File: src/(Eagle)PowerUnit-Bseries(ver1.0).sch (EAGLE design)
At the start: 53 parts, among them CON1 XT90PW-M, CON2 XT90PW-F, CON3 XT60PW-F, CON4 XT60PW-F, CON5 XT60PW-F, CON6 XT60PW-F, U1 LQFP64, U2 MCP2517FD, U3 CH340E, U4 AP63203WU-7

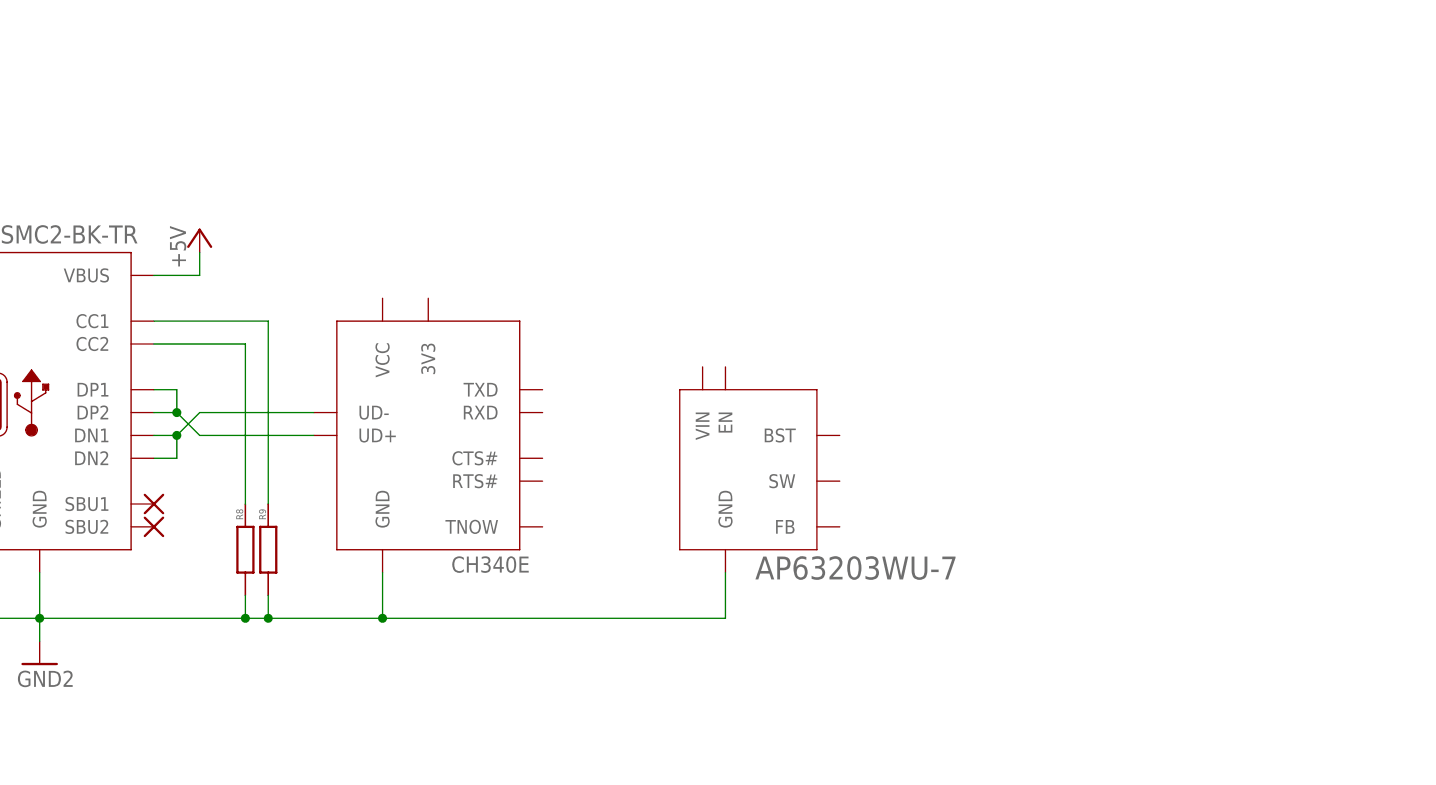
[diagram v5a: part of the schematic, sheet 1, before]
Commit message: 5Vレギュレータの追加など
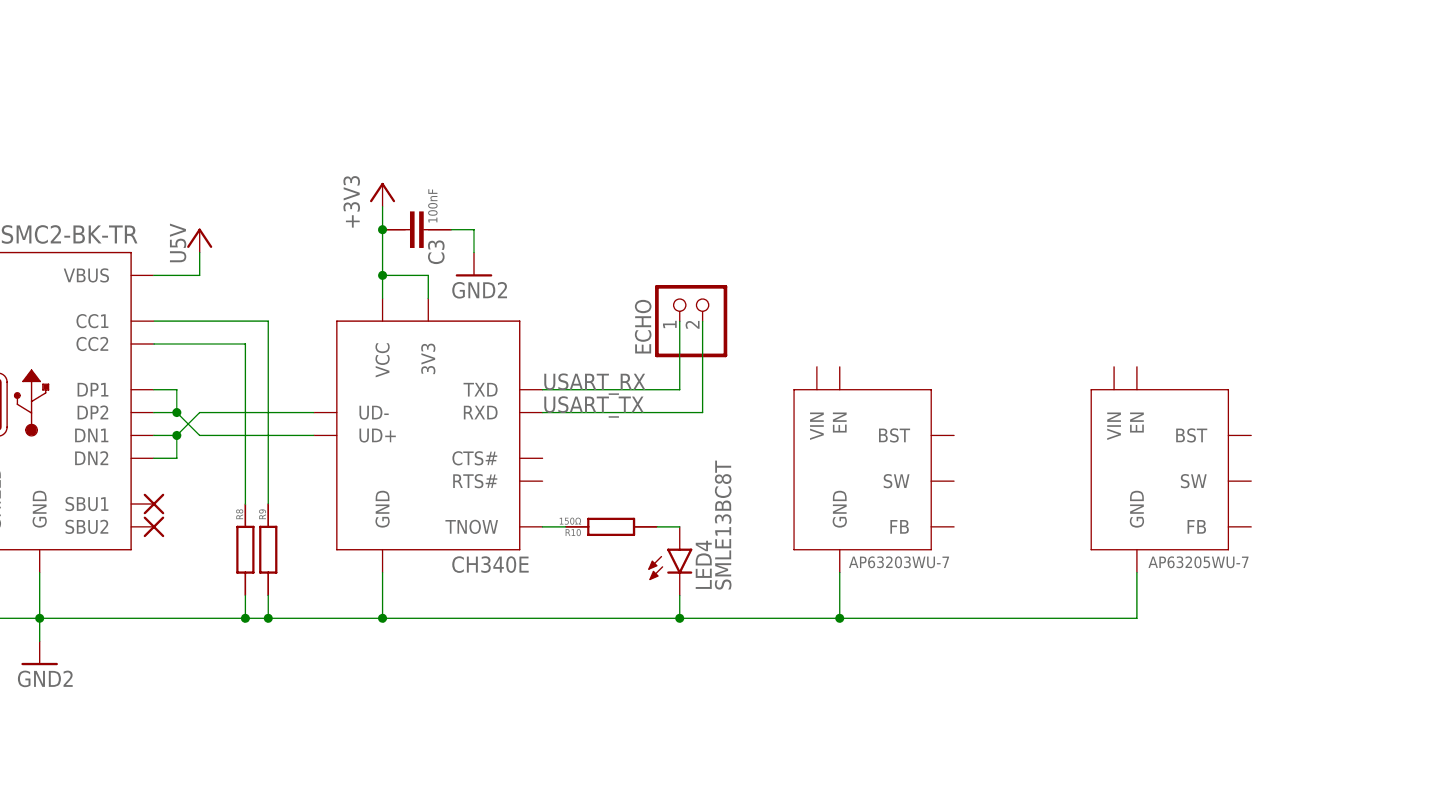
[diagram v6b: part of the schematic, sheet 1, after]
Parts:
- added C3: GCM188L81H104KA57, GCM188L81H104K57(0.1uF):GCM188L81H104KA57
- added ECHO: (no value), pinhead:PINHD-1X2
- added LED4: SMLE13BC8T, SML-E12V8WT86:SML-E12V8WT86
- added R10: 150Ω, CR0603:CR0603
- added U5: AP63205WU-7, AP63205WU-7:AP63205WU-7
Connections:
- net +5V renamed U5V
- new net +3V3: C3.P$2, U3.3V3, U3.VCC
- new net N$33: R10.RIGHT, U3.TNOW
- new net N$34: LED4.A, R10.LEFT
- new net USART_RX: ECHO.1, U1.P17, U3.TXD
- new net USART_TX: ECHO.2, U1.P16, U3.RXD
- net GND2: now also C3.P$1, LED4.C, U5.GND
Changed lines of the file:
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@@
 <part name="U3" library="CH340E" deviceset="CH340E" device=""/>
 <part name="U4" library="AP63203WU-7" deviceset="AP63203WU-7" device=""/>
+<part name="U5" library="AP63205WU-7" deviceset="AP63205WU-7" device=""/>
+<part name="ECHO" library="pinhead" library_urn="urn:adsk.eagle:library:325" deviceset="PINHD-1X2" device="" package3d_urn="urn:adsk.eagle:package:22435/2"/>
+<part name="C3" library="GCM188L81H104K57(0.1uF)" deviceset="GCM188L81H104KA57" device=""/>
+<part name="GND2" library="supply1" library_urn="urn:adsk.eagle:library:371" deviceset="GND" device=""/>
+<part name="+3V1" library="supply1" library_urn="urn:adsk.eagle:library:371" deviceset="+3V3" device=""/>
+<part name="R10" library="CR0603" deviceset="CR0603" device="" value="150Ω"/>
+<part name="LED4" library="SML-E12V8WT86" deviceset="SML-E12V8WT86" device="" value="SMLE13BC8T"/>
 </parts>
 <sheets>
@@
 <instance part="U$2" gate="G$1" x="119.38" y="101.6" smashed="yes"/>
 <instance part="U$3" gate="G$1" x="119.38" y="104.14" smashed="yes"/>
-<instance part="P+5" gate="1" x="124.46" y="134.62" smashed="yes">
-<attribute name="VALUE" x="122.936" y="130.302" size="1.778" layer="96" rot="R90"/>
-</instance>
+<instance part="P+5" gate="1" x="124.46" y="134.62" smashed="yes"/>
 <instance part="R8" gate="G$1" x="129.54" y="99.06" smashed="yes" rot="R90">
 <attribute name="NAME" x="129.286" y="102.362" size="0.762" layer="95" rot="R90"/>
@@
 <attribute name="VALUE" x="152.4" y="96.52" size="1.778" layer="96"/>
 </instance>
-<instance part="U4" gate="G$1" x="177.8" y="99.06" smashed="yes">
-<attribute name="VALUE" x="186.182" y="95.758" size="2.54" layer="96"/>
+<instance part="U4" gate="G$1" x="190.5" y="99.06" smashed="yes">
+<attribute name="VALUE" x="196.596" y="97.028" size="1.27" layer="96"/>
+</instance>
+<instance part="U5" gate="G$1" x="223.52" y="99.06" smashed="yes">
+<attribute name="VALUE" x="229.87" y="97.028" size="1.27" layer="96"/>
+</instance>
+<instance part="ECHO" gate="G$1" x="180.34" y="127" smashed="yes" rot="R90">
+<attribute name="NAME" x="174.625" y="120.65" size="1.778" layer="95" rot="R90"/>
+<attribute name="VALUE" x="185.42" y="120.65" size="1.778" layer="96" rot="R90"/>
+</instance>
+<instance part="C3" gate="G$1" x="149.86" y="134.62" smashed="yes" rot="R270">
+<attribute name="NAME" x="149.86" y="133.604" size="1.778" layer="95" rot="R270"/>
+</instance>
+<instance part="GND2" gate="1" x="154.94" y="129.54" smashed="yes"/>
+<instance part="+3V1" gate="G$1" x="144.78" y="139.7" smashed="yes">
+<attribute name="VALUE" x="142.24" y="134.62" size="1.778" layer="96" rot="R90"/>
+</instance>
+<instance part="R10" gate="G$1" x="170.18" y="101.6" smashed="yes" rot="R180">
+<attribute name="NAME" x="166.878" y="101.346" size="0.762" layer="95" rot="R180"/>
+<attribute name="VALUE" x="166.878" y="102.616" size="0.762" layer="96" rot="R180"/>
+</instance>
+<instance part="LED4" gate="G$1" x="177.8" y="99.06" smashed="yes">
+<attribute name="NAME" x="181.356" y="94.488" size="1.778" layer="95" rot="R90"/>
+<attribute name="VALUE" x="183.515" y="94.488" size="1.778" layer="96" rot="R90"/>
 </instance>
 </instances>
@@
 <label x="104.14" y="83.82" size="1.778" layer="95"/>
 <pinref part="U4" gate="G$1" pin="GND"/>
-<wire x1="144.78" y1="91.44" x2="182.88" y2="91.44" width="0.1524" layer="91"/>
-<wire x1="182.88" y1="91.44" x2="182.88" y2="96.52" width="0.1524" layer="91"/>
+<wire x1="144.78" y1="91.44" x2="177.8" y2="91.44" width="0.1524" layer="91"/>
+<wire x1="177.8" y1="91.44" x2="195.58" y2="91.44" width="0.1524" layer="91"/>
+<wire x1="195.58" y1="91.44" x2="195.58" y2="96.52" width="0.1524" layer="91"/>
 <junction x="144.78" y="91.44"/>
+<pinref part="U5" gate="G$1" pin="GND"/>
+<wire x1="228.6" y1="96.52" x2="228.6" y2="91.44" width="0.1524" layer="91"/>
+<wire x1="228.6" y1="91.44" x2="195.58" y2="91.44" width="0.1524" layer="91"/>
+<junction x="195.58" y="91.44"/>
+<pinref part="LED4" gate="G$1" pin="C"/>
+<wire x1="177.8" y1="93.98" x2="177.8" y2="91.44" width="0.1524" layer="91"/>
+<junction x="177.8" y="91.44"/>
+</segment>
+<segment>
+<pinref part="C3" gate="G$1" pin="P$1"/>
+<wire x1="152.4" y1="134.62" x2="154.94" y2="134.62" width="0.1524" layer="91"/>
+<pinref part="GND2" gate="1" pin="GND"/>
+<wire x1="154.94" y1="134.62" x2="154.94" y2="132.08" width="0.1524" layer="91"/>
+<label x="152.4" y="127" size="1.778" layer="95"/>
 </segment>
 </net>
@@
 </segment>
 </net>
-<net name="+5V" class="0">
+<net name="U5V" class="0">
 <segment>
 <pinref part="USB1" gate="G$1" pin="VBUS"/>
@@
 <wire x1="119.38" y1="129.54" x2="124.46" y2="129.54" width="0.1524" layer="91"/>
 <wire x1="124.46" y1="129.54" x2="124.46" y2="132.08" width="0.1524" layer="91"/>
+<label x="122.936" y="130.81" size="1.778" layer="95" rot="R90"/>
 </segment>
 </net>
@@
 <pinref part="U3" gate="G$1" pin="UD-"/>
 <wire x1="124.46" y1="114.3" x2="137.16" y2="114.3" width="0.1524" layer="91"/>
+</segment>
+</net>
+<net name="USART_RX" class="0">
+<segment>
+<pinref part="U3" gate="G$1" pin="TXD"/>
+<wire x1="162.56" y1="116.84" x2="177.8" y2="116.84" width="0.1524" layer="91"/>
+<label x="162.56" y="116.84" size="1.778" layer="95"/>
+<pinref part="ECHO" gate="G$1" pin="1"/>
+<wire x1="177.8" y1="116.84" x2="177.8" y2="124.46" width="0.1524" layer="91"/>
+</segment>
+</net>
+<net name="USART_TX" class="0">
+<segment>
+<pinref part="U3" gate="G$1" pin="RXD"/>
+<wire x1="162.56" y1="114.3" x2="180.34" y2="114.3" width="0.1524" layer="91"/>
+<label x="162.56" y="114.3" size="1.778" layer="95"/>
+<pinref part="ECHO" gate="G$1" pin="2"/>
+<wire x1="180.34" y1="114.3" x2="180.34" y2="124.46" width="0.1524" layer="91"/>
+</segment>
+</net>
+<net name="+3V3" class="0">
+<segment>
+<pinref part="U3" gate="G$1" pin="VCC"/>
+<wire x1="144.78" y1="127" x2="144.78" y2="129.54" width="0.1524" layer="91"/>
+<wire x1="144.78" y1="129.54" x2="149.86" y2="129.54" width="0.1524" layer="91"/>
+<pinref part="U3" gate="G$1" pin="3V3"/>
+<wire x1="149.86" y1="129.54" x2="149.86" y2="127" width="0.1524" layer="91"/>
+<pinref part="C3" gate="G$1" pin="P$2"/>
+<wire x1="144.78" y1="129.54" x2="144.78" y2="134.62" width="0.1524" layer="91"/>
+<junction x="144.78" y="129.54"/>
+<pinref part="+3V1" gate="G$1" pin="+3V3"/>
+<wire x1="144.78" y1="137.16" x2="144.78" y2="134.62" width="0.1524" layer="91"/>
+<junction x="144.78" y="134.62"/>
+</segment>
+</net>
+<net name="N$33" class="0">
+<segment>
+<pinref part="R10" gate="G$1" pin="RIGHT"/>
+<pinref part="U3" gate="G$1" pin="TNOW"/>
+<wire x1="165.1" y1="101.6" x2="162.56" y2="101.6" width="0.1524" layer="91"/>
+</segment>
+</net>
+<net name="N$34" class="0">
+<segment>
+<pinref part="R10" gate="G$1" pin="LEFT"/>
+<pinref part="LED4" gate="G$1" pin="A"/>
+<wire x1="175.26" y1="101.6" x2="177.8" y2="101.6" width="0.1524" layer="91"/>
 </segment>
 </net>
@@
 </busses>
 <nets>
+<net name="USART_TX" class="0">
+<segment>
+<pinref part="U1" gate="G$1" pin="P16"/>
+<wire x1="106.68" y1="68.58" x2="88.9" y2="68.58" width="0.1524" layer="91"/>
+<label x="88.9" y="68.58" size="1.778" layer="95"/>
+</segment>
+</net>
+<net name="USART_RX" class="0">
+<segment>
+<pinref part="U1" gate="G$1" pin="P17"/>
+<wire x1="109.22" y1="63.5" x2="109.22" y2="43.18" width="0.1524" layer="91"/>
+<label x="109.22" y="43.18" size="1.778" layer="95" rot="R90"/>
+</segment>
+</net>
 </nets>
 </sheet>

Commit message: 理想ダイオード回路(ディスクリート)の追加
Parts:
- added GND, POW1: (no value), pinhead:PINHD-1X2
- added POW: 02-JST, con-jst-xh:02-JST
- added Q1, Q2, Q3: DMP3056L-7, DMP3056L-7:DMP3056L-7
- added R11, R12, R13, R14, R15, R18, R19, R20, R21, R22, R25, R26, R27, R28, R29: 10k, CR0603:CR0603
- added R16, R23, R30: 100k, CR0603:CR0603
- added R17, R24, R31: 0, CR0603:CR0603
- added U6, U7, U8: AP331AWG-7, AP331AWG-7:AP331AWG-7
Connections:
- new net N$35: POW1.2, Q1.DRAIN, R12.RIGHT
- new net N$37: Q1.GATE, R11.RIGHT, R16.LEFT, R17.LEFT, R17.RIGHT, U6.OUTPUT
- new net N$38: R12.LEFT, R13.RIGHT, U6.IN-
- new net N$39: R14.LEFT, R15.RIGHT, U6.IN+
- new net N$41: Q2.GATE, R18.RIGHT, R23.LEFT, R24.LEFT, R24.RIGHT, U7.OUTPUT
- new net N$43: R19.LEFT, R20.RIGHT, U7.IN-
- new net N$44: R21.LEFT, R22.RIGHT, U7.IN+
- new net N$45: POW.2, Q3.DRAIN, R26.RIGHT
- new net N$46: Q3.GATE, R25.RIGHT, R30.LEFT, R31.LEFT, R31.RIGHT, U8.OUTPUT
- new net N$48: R26.LEFT, R27.RIGHT, U8.IN-
- new net N$49: R28.LEFT, R29.RIGHT, U8.IN+
- new net V+: Q1.SOURCE, Q2.SOURCE, Q3.SOURCE, R11.LEFT, R14.RIGHT, R16.RIGHT, R18.LEFT, R21.RIGHT, R23.RIGHT, R25.LEFT, R28.RIGHT, R30.RIGHT, U6.VCC, U7.VCC, U8.VCC
- net GND: now also GND.2
- net GND2: now also GND.1, POW.1, R13.LEFT, R15.LEFT, R20.LEFT, R22.LEFT, R27.LEFT, R29.LEFT, U6.GND, U7.GND, U8.GND
- net U5V: now also Q2.DRAIN, R19.RIGHT
- net VCC: now also POW1.1
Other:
- moved on the sheet: C3, CON3, CON4, CON5, CON6, ECHO, EDGE1, EDGE2, EDGE3, EDGE4, IRLB-1, IRLB-2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

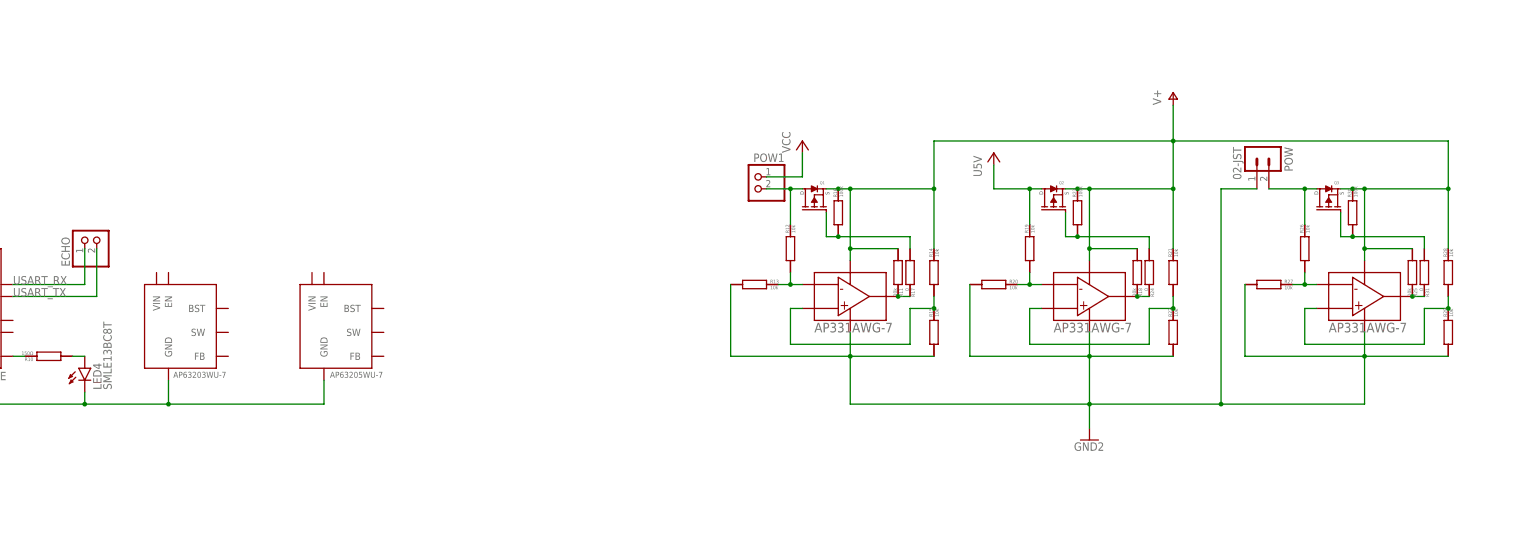
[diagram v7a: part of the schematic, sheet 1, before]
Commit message: 5VDCDCのMLCC選定、電源回りの整理
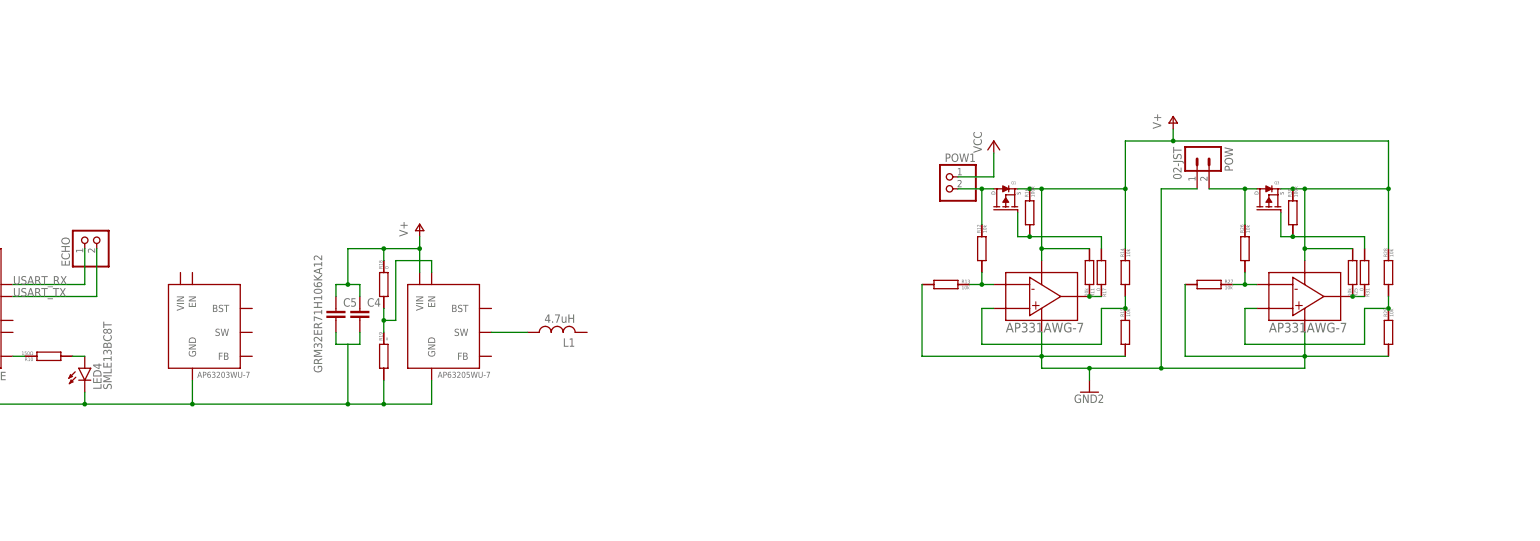
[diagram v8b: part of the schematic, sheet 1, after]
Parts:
- removed Q2: DMP3056L-7, DMP3056L-7:DMP3056L-7
- removed R20, R21, R22: 10k, CR0603:CR0603
- removed R23: 100k, CR0603:CR0603
- removed R24: 0, CR0603:CR0603
- removed U7: AP331AWG-7, AP331AWG-7:AP331AWG-7
- added C4, C5: GRM32ER71H106KA12, GRM32ER71H106KA12:GRM32ER71H106KA12
- added L1: 4.7uH, NRS5030T4R7MMGJ:NRS5030T4R7MMGJ
- R18: value 10k -> 0
- R19: value 10k -> ∞
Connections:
- removed net N$41: Q2.GATE, R18.RIGHT, R23.LEFT, R24.LEFT, R24.RIGHT, U7.OUTPUT
- removed net N$43: R19.LEFT, R20.RIGHT, U7.IN-
- removed net N$44: R21.LEFT, R22.RIGHT, U7.IN+
- new net N$36: R18.LEFT, R19.RIGHT, U5.EN
- new net N$40: L1.L, U5.SW
- net GND2: now also C4.R, C5.R, R19.LEFT; no longer R20.LEFT, R22.LEFT, U7.GND
- net U5V: no longer Q2.DRAIN, R19.RIGHT
- net V+: now also C4.L, C5.L, R18.RIGHT, U5.VIN; no longer Q2.SOURCE, R18.LEFT, R21.RIGHT, R23.RIGHT, U7.VCC
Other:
- moved on the sheet: POW, POW1, Q1, Q3, R11, R12, R13, R14, R15, R16, R17, R18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
